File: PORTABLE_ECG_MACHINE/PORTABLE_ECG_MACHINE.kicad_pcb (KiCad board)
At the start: 2 copper layers, 25.5 x 64.8 mm, 79 parts, among them IC1 AD8232ACPZ, J1 UART, J2 AudioJack3, J3 Li-Ion 3.7 CONN, J4 USB_C_Receptacle_USB2.0, Q1 BSS138, Q2 BSS138, SW1 SW_SPDT, U1 SSD1306, U2 CP2102-GM, U3 TC1262-33, U4 TP4056

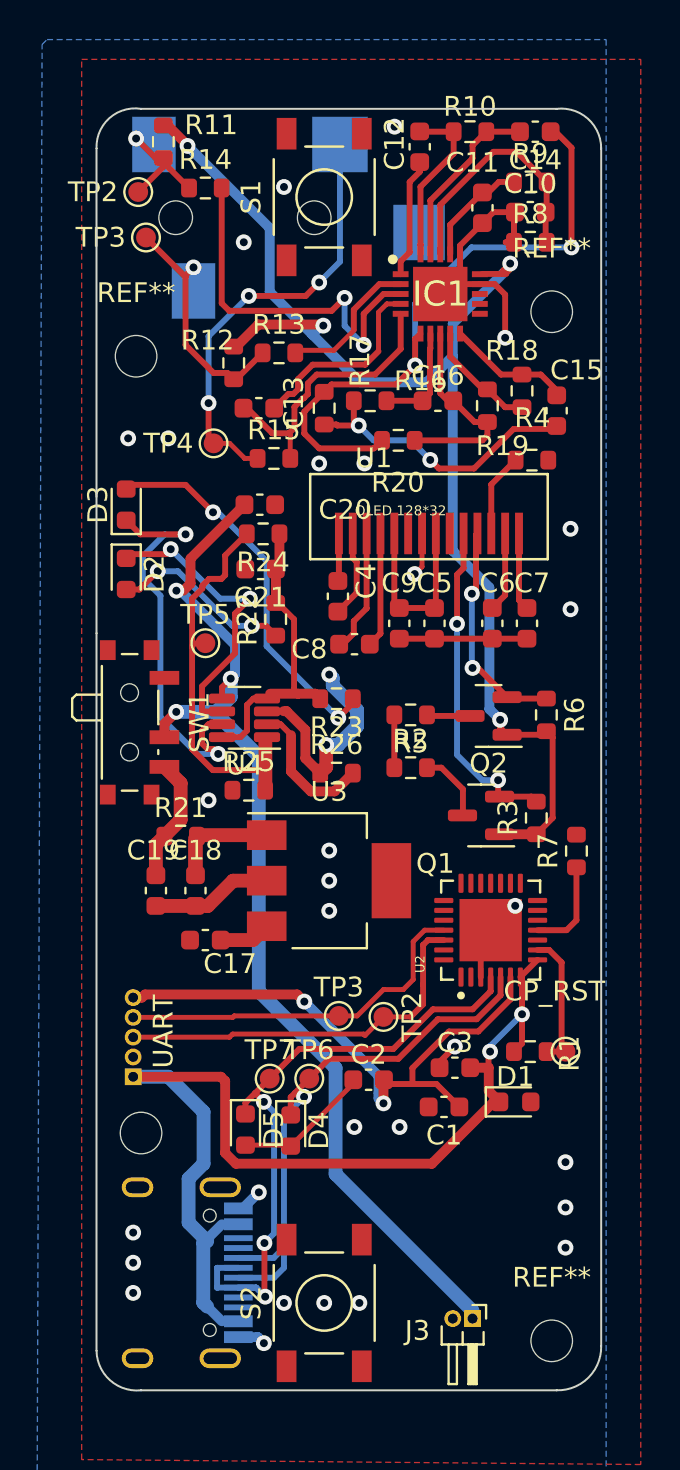
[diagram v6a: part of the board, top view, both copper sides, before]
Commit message: OLED 3D change | uC add | .step gen v4
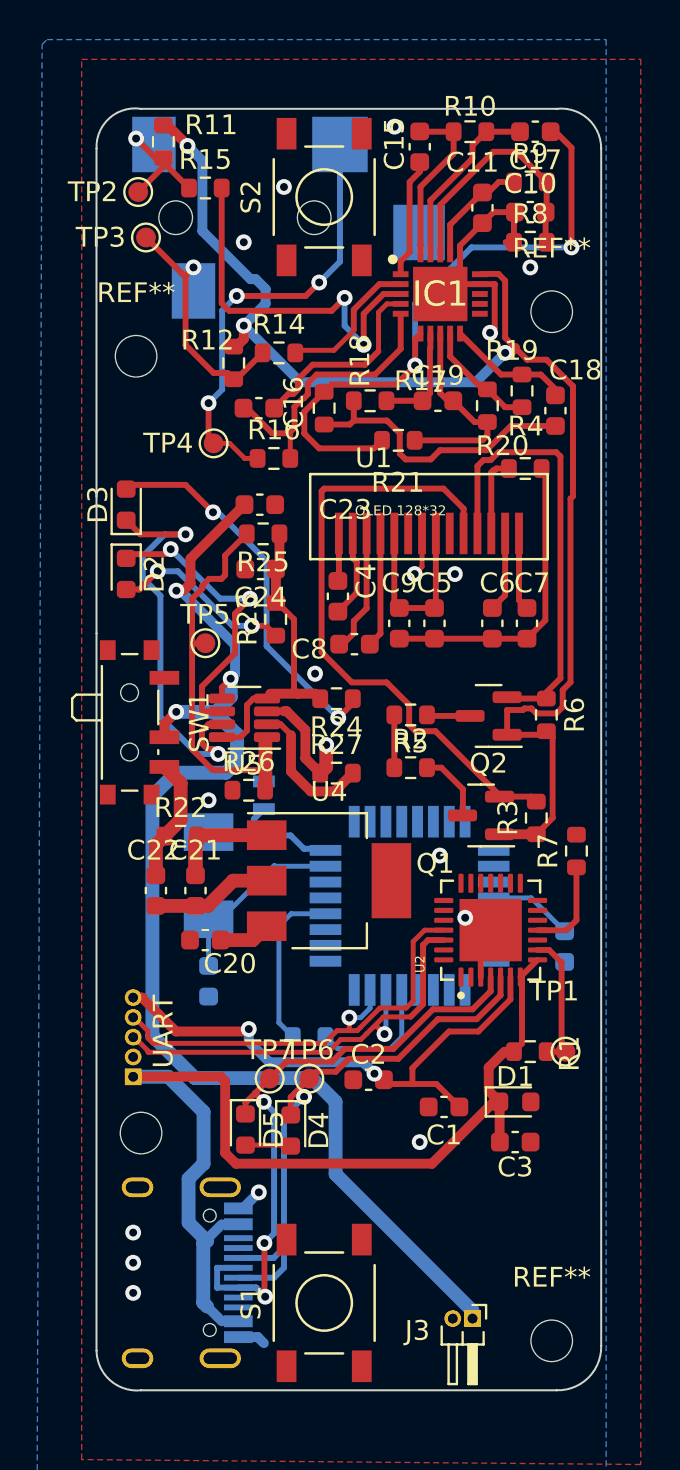
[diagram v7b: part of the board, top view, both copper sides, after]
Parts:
- removed the TP2 at (98.5, 70.4)
- removed the TP3 at (96.2, 70.3)
- added C12: .1uf, Capacitor_SMD:C_0603_1608Metric, B.Cu at (107.7, 66.8)
- added C13: 10p, Capacitor_SMD:C_0603_1608Metric, B.Cu at (89.7, 68.6)
- added C14: 10p, Crystal:Crystal_SMD_2012-2Pin_2.0x1.2mm, B.Cu at (92.5, 59.2)
- added R13: 10K, Resistor_SMD:R_0603_1608Metric, B.Cu at (94.7, 71.4)
- added U3: ATmega328PB-A, Package_QFP:TQFP-32_7x7mm_P0.8mm, B.Cu at (99.8, 64.8)
- added Y1: 16MHZ, Crystal:Crystal_SMD_0603-2Pin_6.0x3.5mm, B.Cu at (89.7, 63.2)
- moved C3 4.84 mm to (105.2, 76.7), turned to 0 degrees
- moved R4 0.54 mm to (105.7, 42.7)
- moved C18 0.06 mm to (107.2, 39.8)
- renumbered C12 to C15, C13 to C16, C14 to C17, C15 to C18, C16 to C19, C17 to C20, C18 to C21, C19 to C22, C20 to C23, C21 to C24, R13 to R14, R14 to R15, R15 to R16, R16 to R17, R17 to R18, R18 to R19, R19 to R20, R20 to R21, R21 to R22, R22 to R23, R23 to R24, R24 to R25, R25 to R26, R26 to R27, S2 to S1, S1 to S2, CP_RST to TP1, U3 to U4, U4 to U5
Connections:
- S1 pad 3: unconnected-(S2-Pad3) (its old number) -> Net-(S1-Pad3)
- S2 pad 4: unconnected-(S1-Pad4) (its old number) -> Net-(S2-Pad4)
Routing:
- net SCL_3.3: track 16.8 -> 31.6 mm, vias 2 -> 0
- net SDA_3.3: track 11.3 -> 22.4 mm, vias 2 -> 0
- net Net-(C13-Pad1): track 0.00 -> 9.40 mm
- net /BATTERY +VE: track 56.6 -> 65.1 mm
- net VCC: track 6.33 -> 14.8 mm
- net Net-(C14-Pad1): track 0.00 -> 7.84 mm
- net /RST#: track 0.00 -> 6.73 mm
- net /RXD: track 18.6 -> 23.4 mm, vias 0 -> 1
- net Net-(C12-Pad2): track 0.00 -> 4.28 mm
- net /TXD: track 19.5 -> 23.0 mm, vias 0 -> 1
- net 3.3V: track 65.7 -> 69.0 mm, vias 4 -> 3
- net GND: track 54.4 -> 52.1 mm, vias 32 -> 17
- net Net-(C1-Pad1): track 29.6 -> 27.6 mm
- net VIN: track 56.1 -> 55.4 mm, vias 2 -> 0
- net Net-(C18-Pad2): vias 2 -> 0

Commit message: Conn complete | DRC CHECK2 | TEST INITIATE #V6#
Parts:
- moved C14 0.72 mm to (93.0, 58.7), turned to 180 degrees
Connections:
- S2 pad 3: unconnected-(S2-Pad3) -> Net-(S2-Pad3)
- S2 pad 4: Net-(S2-Pad4) -> unconnected-(S2-Pad4)
- U3 pad 1: Net-(S2-Pad4) -> unconnected-(U3-Pad1)
- U3 pad 11: unconnected-(U3-Pad11) -> Net-(S2-Pad3)
- U3 pad 26: unconnected-(U3-Pad26) -> Net-(S1-Pad3)
- U3 pad 32: Net-(S1-Pad3) -> unconnected-(U3-Pad32)
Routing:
- net Net-(S2-Pad3): track 0.00 -> 50.1 mm, vias 0 -> 1
- net +3V3: track 2.61 -> 26.2 mm, vias 0 -> 1
- net Net-(S1-Pad3): track 0.00 -> 22.7 mm, vias 0 -> 1
- net VCC: track 14.8 -> 28.6 mm, vias 0 -> 1
- net GND: track 52.1 -> 54.8 mm, vias 17 -> 24
- net Net-(C14-Pad1): track 7.84 -> 10.1 mm
- net 3.3V: track 69.0 -> 69.6 mm
- net Net-(IC1-Pad3): track 19.1 -> 19.7 mm
